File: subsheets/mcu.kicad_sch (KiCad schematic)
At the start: 25 parts, among them J2 Conn_02x12_Top_Bottom, U5 LoRa-E5

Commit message: PCB edits
-
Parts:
- removed J2: Conn_02x12_Top_Bottom, Connector_PinHeader_2.54mm:PinHeader_2x12_P2.54mm_Vertical, symbol Connector_Generic:Conn_02x12_Top_Bottom
- added J2: Conn_01x05, Connector_PinHeader_1.27mm:PinHeader_1x05_P1.27mm_Vertical, symbol Connector_Generic:Conn_01x05
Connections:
- net GND: now also J2.3 (Pin_3)
- net PA13/SWDIO: now also J2.1 (Pin_1)
- net PA14/SWCLK: now also J2.2 (Pin_2)
- net RST: now also J2.4 (Pin_4)
- net PA13/SCK renamed PB13/SCK

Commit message: PCB Routed
-
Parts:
- J2: footprint Connector_PinHeader_1.27mm:PinHeader_1x05_P1.27mm_Vertical -> 2X10_BOXHEADER; symbol Connector_Generic:Conn_01x05 -> SWD:SWD
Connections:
- net +3.3V: now also J2.1 (VDD)
- net GND: now also J2.5 (GND@1), J2.9 (GND_DETECT)
- net PA13/SWDIO: now also J2.2 (SWDIO); no longer J2.1 (Pin_1)
- net PA14/SWCLK: now also J2.4 (SWDCLK); no longer J2.2 (Pin_2)
- net RST: now also J2.10 (RESET); no longer J2.4 (Pin_4)
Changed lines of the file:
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@@
   (junction (at 66.04 77.47) (diameter 0) (color 0 0 0 0)
   )
+  (junction (at 151.13 143.51) (diameter 0) (color 0 0 0 0)
+  )
   (junction (at 81.28 50.8) (diameter 0) (color 0 0 0 0)
   )
@@
     (stroke (width 0) (type default) (color 0 0 0 0))
   )
-  (wire (pts (xy 128.27 144.78) (xy 129.54 144.78))
-    (stroke (width 0) (type default) (color 0 0 0 0))
-  )
   (wire (pts (xy 153.67 68.58) (xy 160.02 68.58))
     (stroke (width 0) (type default) (color 0 0 0 0))
@@
     (stroke (width 0) (type default) (color 0 0 0 0))
   )
+  (wire (pts (xy 151.13 143.51) (xy 151.13 144.78))
+    (stroke (width 0) (type default) (color 0 0 0 0))
+  )
   (wire (pts (xy 43.18 165.1) (xy 43.18 170.18))
     (stroke (width 0) (type default) (color 0 0 0 0))
@@
     (stroke (width 0) (type default) (color 0 0 0 0))
   )
+  (wire (pts (xy 151.13 143.51) (xy 153.67 143.51))
+    (stroke (width 0) (type default) (color 0 0 0 0))
+  )
   (wire (pts (xy 133.35 42.545) (xy 133.35 45.72))
     (stroke (width 0) (type default) (color 0 0 0 0))
@@
     (stroke (width 0) (type default) (color 0 0 0 0))
   )
+  (wire (pts (xy 151.13 149.86) (xy 153.67 149.86))
+    (stroke (width 0) (type default) (color 0 0 0 0))
+  )
   (wire (pts (xy 69.85 77.47) (xy 66.04 77.47))
     (stroke (width 0) (type default) (color 0 0 0 0))
@@
     (stroke (width 0) (type default) (color 0 0 0 0))
   )
+  (wire (pts (xy 151.13 142.24) (xy 151.13 143.51))
+    (stroke (width 0) (type default) (color 0 0 0 0))
+  )
   (wire (pts (xy 33.655 100.33) (xy 52.07 100.33))
     (stroke (width 0) (type default) (color 0 0 0 0))
@@
     (stroke (width 0) (type default) (color 0 0 0 0))
   )
-  (wire (pts (xy 128.27 147.32) (xy 129.54 147.32))
-    (stroke (width 0) (type default) (color 0 0 0 0))
-  )
-  (wire (pts (xy 128.27 142.24) (xy 129.54 142.24))
+  (wire (pts (xy 116.84 142.24) (xy 118.11 142.24))
     (stroke (width 0) (type default) (color 0 0 0 0))
   )
@@
     (stroke (width 0) (type default) (color 0 0 0 0))
   )
+  (wire (pts (xy 116.84 139.7) (xy 118.11 139.7))
+    (stroke (width 0) (type default) (color 0 0 0 0))
+  )
   (wire (pts (xy 49.53 63.5) (xy 49.53 69.85))
     (stroke (width 0) (type default) (color 0 0 0 0))
@@
     (stroke (width 0) (type default) (color 0 0 0 0))
   )
+  (wire (pts (xy 151.13 139.7) (xy 152.4 139.7))
+    (stroke (width 0) (type default) (color 0 0 0 0))
+  )
   (wire (pts (xy 153.67 63.5) (xy 155.575 63.5))
     (stroke (width 0) (type default) (color 0 0 0 0))
@@
     (stroke (width 0) (type default) (color 0 0 0 0))
   )
+  (wire (pts (xy 116.84 149.86) (xy 118.11 149.86))
+    (stroke (width 0) (type default) (color 0 0 0 0))
+  )
   (wire (pts (xy 49.53 140.97) (xy 49.53 153.67))
     (stroke (width 0) (type default) (color 0 0 0 0))
@@
   )
   (wire (pts (xy 104.14 166.37) (xy 106.68 166.37))
-    (stroke (width 0) (type default) (color 0 0 0 0))
-  )
-  (wire (pts (xy 128.27 139.7) (xy 129.54 139.7))
     (stroke (width 0) (type default) (color 0 0 0 0))
   )
@@
     )
   )
+  (global_label "+3.3V" (shape input) (at 152.4 139.7 0) (fields_autoplaced)
+    (effects (font (size 1 1)) (justify left))
+    (property "Intersheet References" "${INTERSHEET_REFS}" (id 0) (at 158.7762 139.6375 0)
+      (effects (font (size 1 1)) (justify left) hide)
+    )
+  )
   (global_label "PA10{slash}MOSI" (shape input) (at 130.81 42.545 90) (fields_autoplaced)
     (effects (font (size 1 1)) (justify left))
@@
     )
   )
-  (global_label "PA13{slash}SWDIO" (shape input) (at 128.27 139.7 180) (fields_autoplaced)
-    (effects (font (size 1 1)) (justify right))
-    (property "Intersheet References" "${INTERSHEET_REFS}" (id 0) (at 116.9414 139.6375 0)
-      (effects (font (size 1 1)) (justify right) hide)
-    )
-  )
-  (global_label "PA14{slash}SWCLK" (shape input) (at 128.27 142.24 180) (fields_autoplaced)
-    (effects (font (size 1 1)) (justify right))
-    (property "Intersheet References" "${INTERSHEET_REFS}" (id 0) (at 116.6557 142.1775 0)
+  (global_label "PA13{slash}SWDIO" (shape input) (at 116.84 139.7 180) (fields_autoplaced)
+    (effects (font (size 1 1)) (justify right))
+    (property "Intersheet References" "${INTERSHEET_REFS}" (id 0) (at 105.5114 139.6375 0)
+      (effects (font (size 1 1)) (justify right) hide)
+    )
+  )
+  (global_label "PA14{slash}SWCLK" (shape input) (at 116.84 142.24 180) (fields_autoplaced)
+    (effects (font (size 1 1)) (justify right))
+    (property "Intersheet References" "${INTERSHEET_REFS}" (id 0) (at 105.2257 142.1775 0)
       (effects (font (size 1 1)) (justify right) hide)
     )
@@
     )
   )
-  (global_label "RST" (shape input) (at 128.27 147.32 180) (fields_autoplaced)
-    (effects (font (size 1 1)) (justify right))
-    (property "Intersheet References" "${INTERSHEET_REFS}" (id 0) (at 123.6557 147.3825 0)
+  (global_label "RST" (shape input) (at 116.84 149.86 180) (fields_autoplaced)
+    (effects (font (size 1 1)) (justify right))
+    (property "Intersheet References" "${INTERSHEET_REFS}" (id 0) (at 112.2257 149.9225 0)
       (effects (font (size 1 1)) (justify right) hide)
     )
@@
     (pin "2")
   )
-  (symbol (lib_id "power:GND") (at 128.27 144.78 270) (unit 1)
+  (symbol (lib_id "power:GND") (at 153.67 149.86 90) (unit 1)
     (in_bom yes) (on_board yes)
-    (property "Reference" "#PWR038" (id 0) (at 121.92 144.78 0)
-      (effects (font (size 1.27 1.27)) hide)
-    )
-    (property "Value" "GND" (id 1) (at 120.65 144.78 90)
-      (effects (font (size 1.27 1.27)) (justify left))
-    )
-    (property "Footprint" "" (id 2) (at 128.27 144.78 0)
-      (effects (font (size 1.27 1.27)) hide)
-    )
-    (property "Datasheet" "" (id 3) (at 128.27 144.78 0)
+    (property "Reference" "#PWR0101" (id 0) (at 160.02 149.86 0)
+      (effects (font (size 1.27 1.27)) hide)
+    )
+    (property "Value" "GND" (id 1) (at 161.29 149.86 90)
+      (effects (font (size 1.27 1.27)) (justify left))
+    )
+    (property "Footprint" "" (id 2) (at 153.67 149.86 0)
+      (effects (font (size 1.27 1.27)) hide)
+    )
+    (property "Datasheet" "" (id 3) (at 153.67 149.86 0)
+      (effects (font (size 1.27 1.27)) hide)
+    )
+    (pin "1")
+  )
+  (symbol (lib_id "power:GND") (at 153.67 143.51 90) (unit 1)
+    (in_bom yes) (on_board yes)
+    (property "Reference" "#PWR038" (id 0) (at 160.02 143.51 0)
+      (effects (font (size 1.27 1.27)) hide)
+    )
+    (property "Value" "GND" (id 1) (at 161.29 143.51 90)
+      (effects (font (size 1.27 1.27)) (justify left))
+    )
+    (property "Footprint" "" (id 2) (at 153.67 143.51 0)
+      (effects (font (size 1.27 1.27)) hide)
+    )
+    (property "Datasheet" "" (id 3) (at 153.67 143.51 0)
       (effects (font (size 1.27 1.27)) hide)
     )
@@
     (pin "2")
   )
-  (symbol (lib_id "Connector_Generic:Conn_01x05") (at 134.62 144.78 0) (unit 1)
-    (in_bom yes) (on_board yes) (fields_autoplaced)
-    (property "Reference" "J2" (id 0) (at 136.652 143.8715 0)
-      (effects (font (size 1.27 1.27)) (justify left))
-    )
-    (property "Value" "Conn_01x05" (id 1) (at 136.652 146.6466 0)
-      (effects (font (size 1.27 1.27)) (justify left))
-    )
-    (property "Footprint" "Connector_PinHeader_1.27mm:PinHeader_1x05_P1.27mm_Vertical" (id 2) (at 134.62 144.78 0)
-      (effects (font (size 1.27 1.27)) hide)
+  (symbol (lib_id "SWD:SWD") (at 134.62 144.78 0) (unit 1)
+    (in_bom yes) (on_board yes)
+    (property "Reference" "J2" (id 0) (at 134.62 143.51 0)
+      (effects (font (size 1.27 1.27)) (justify left))
+    )
+    (property "Value" "Conn_01x05" (id 1) (at 129.54 146.05 0)
+      (effects (font (size 1.27 1.27)) (justify left))
+    )
+    (property "Footprint" "2X10_BOXHEADER" (id 2) (at 134.62 144.78 0)
+      (effects (font (size 1.27 1.27)) (justify left bottom) hide)
     )
     (property "Datasheet" "~" (id 3) (at 134.62 144.78 0)
-      (effects (font (size 1.27 1.27)) hide)
-    )
-    (pin "1")
+      (effects (font (size 1.27 1.27)) (justify left bottom) hide)
+    )
+    (pin "1")
+    (pin "10")
     (pin "2")
     (pin "3")
     (pin "4")
     (pin "5")
+    (pin "6")
+    (pin "7")
+    (pin "8")
+    (pin "9")
   )
   (symbol (lib_id "power:+5V") (at 40.64 148.59 0) (unit 1)

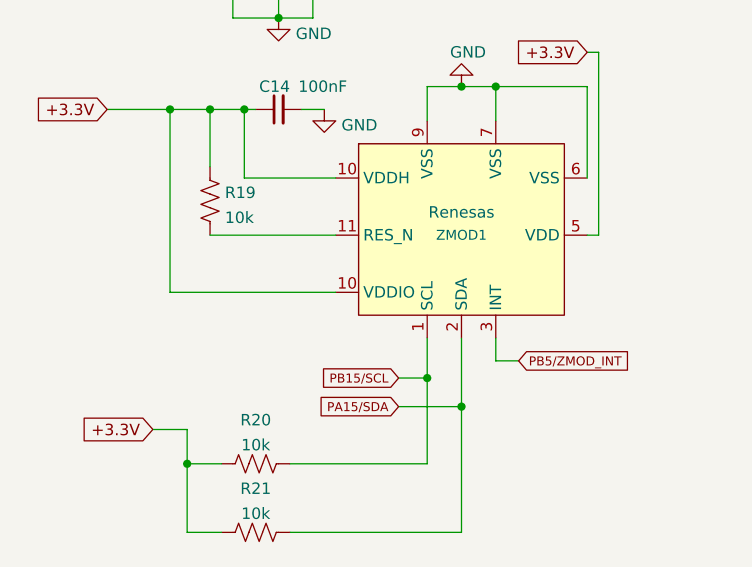
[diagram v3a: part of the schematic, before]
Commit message: DRC runs with 0 Errors. Updates connections and footprints.
-
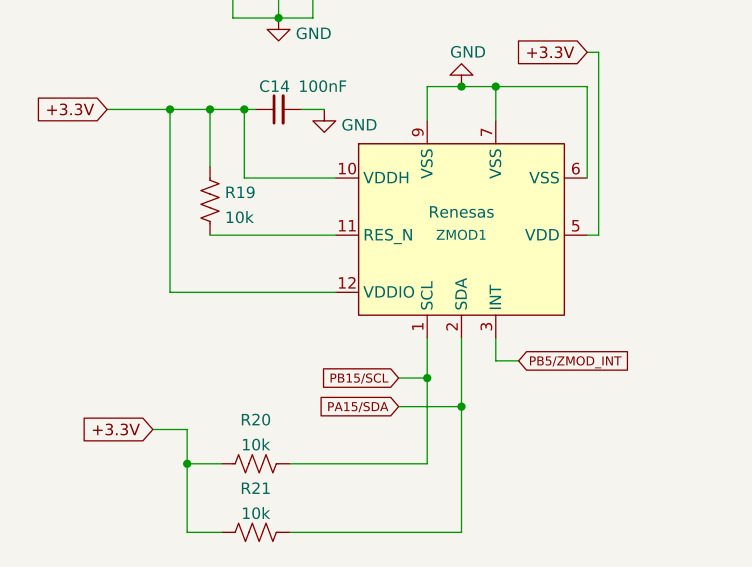
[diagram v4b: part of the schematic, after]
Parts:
- J2: footprint 2X10_BOXHEADER -> Aether:2X10_BOXHEADER
- ZMOD1: footprint Package_LGA:LGA-12_2x2mm_P0.5mm -> Aether:ZMOD4510
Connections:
- net +3.3V: now also ZMOD1.12 (VDDIO)
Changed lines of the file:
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@@
     )
     (property "Value" "Renesas" (id 1) (at 66.04 91.44 0))
-    (property "Footprint" "Package_LGA:LGA-12_2x2mm_P0.5mm" (id 2) (at 66.04 90.17 0)
+    (property "Footprint" "Aether:ZMOD4510" (id 2) (at 66.04 90.17 0)
       (effects (font (size 1.27 1.27)) hide)
     )
@@
     (pin "1")
     (pin "10")
-    (pin "10")
+    (pin "12")
     (pin "11")
     (pin "2")
@@
       (effects (font (size 1.27 1.27)) (justify left))
     )
-    (property "Footprint" "2X10_BOXHEADER" (id 2) (at 134.62 144.78 0)
+    (property "Footprint" "Aether:2X10_BOXHEADER" (id 2) (at 134.62 144.78 0)
       (effects (font (size 1.27 1.27)) (justify left bottom) hide)
     )

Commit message: ZMOD Changes made
-
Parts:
- removed C14: 100nF, Capacitor_SMD:C_0805_2012Metric_Pad1.18x1.45mm_HandSolder, symbol Device:C_Small
- removed R19, R20, R21: 10k, Resistor_SMD:R_0805_2012Metric_Pad1.20x1.40mm_HandSolder, symbol Device:R_US
- removed ZMOD1: Renesas, Aether:ZMOD4510, symbol sensors:Renesas
- added J2: ZMOD4510, Connector_JST:JST_XH_B4B-XH-A_1x04_P2.50mm_Vertical, symbol sensors:ZMOD4510
- renumbered C15 to C14, C16 to C15, J2 to J3, R22 to R19, R23 to R20, R24 to R21, R25 to R22, R26 to R23
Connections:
- net +3.3V: now also J2.4 (3V3)
- net GND: now also J2.1 (GND)
- net PA2/TX2: now also J2.2 (TXD)
- net PA3/RX2: now also J2.3 (RXD)
- net PB5/ZMOD_INT renamed PB5
